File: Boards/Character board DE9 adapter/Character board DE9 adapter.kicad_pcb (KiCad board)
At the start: 2 copper layers, 22.1 x 35.3 mm, 3 parts, among them J1 DE9_Plug_MountingHoles, J2 character connector

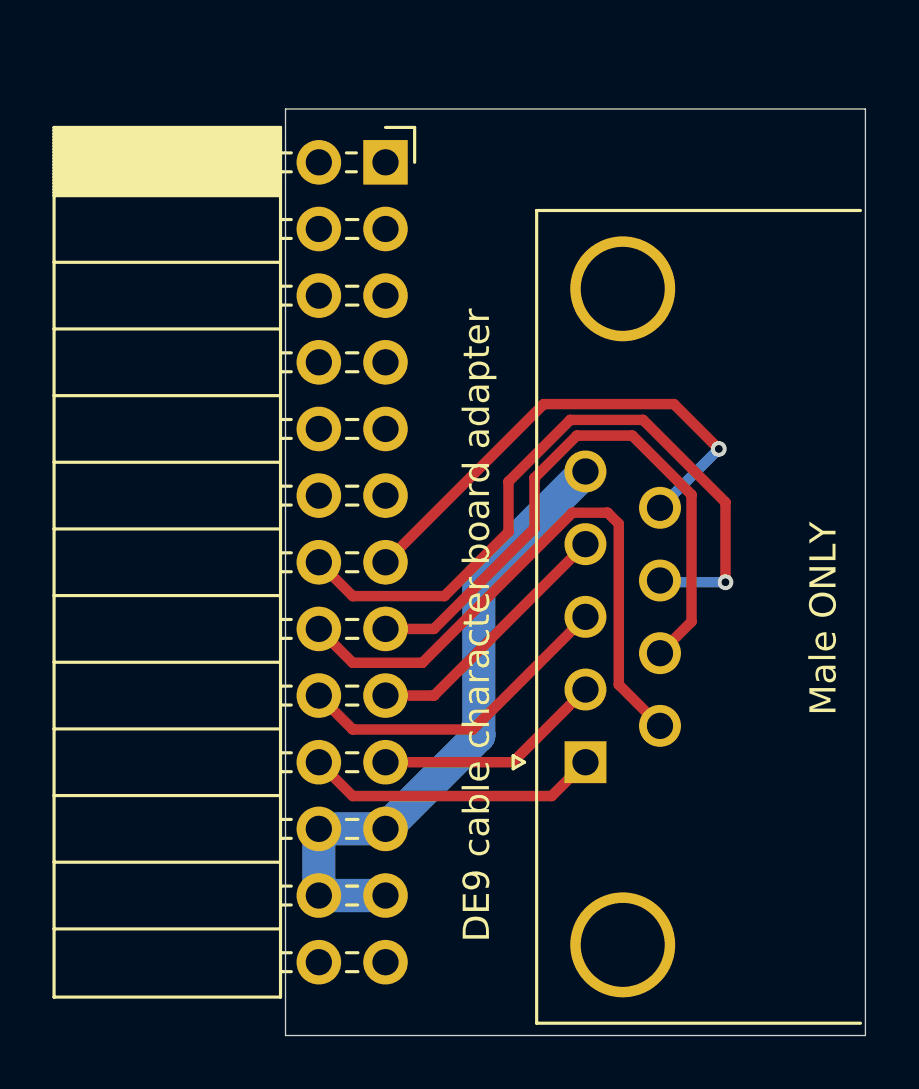
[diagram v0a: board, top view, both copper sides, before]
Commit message: added audio board schematics and de9 board fab files
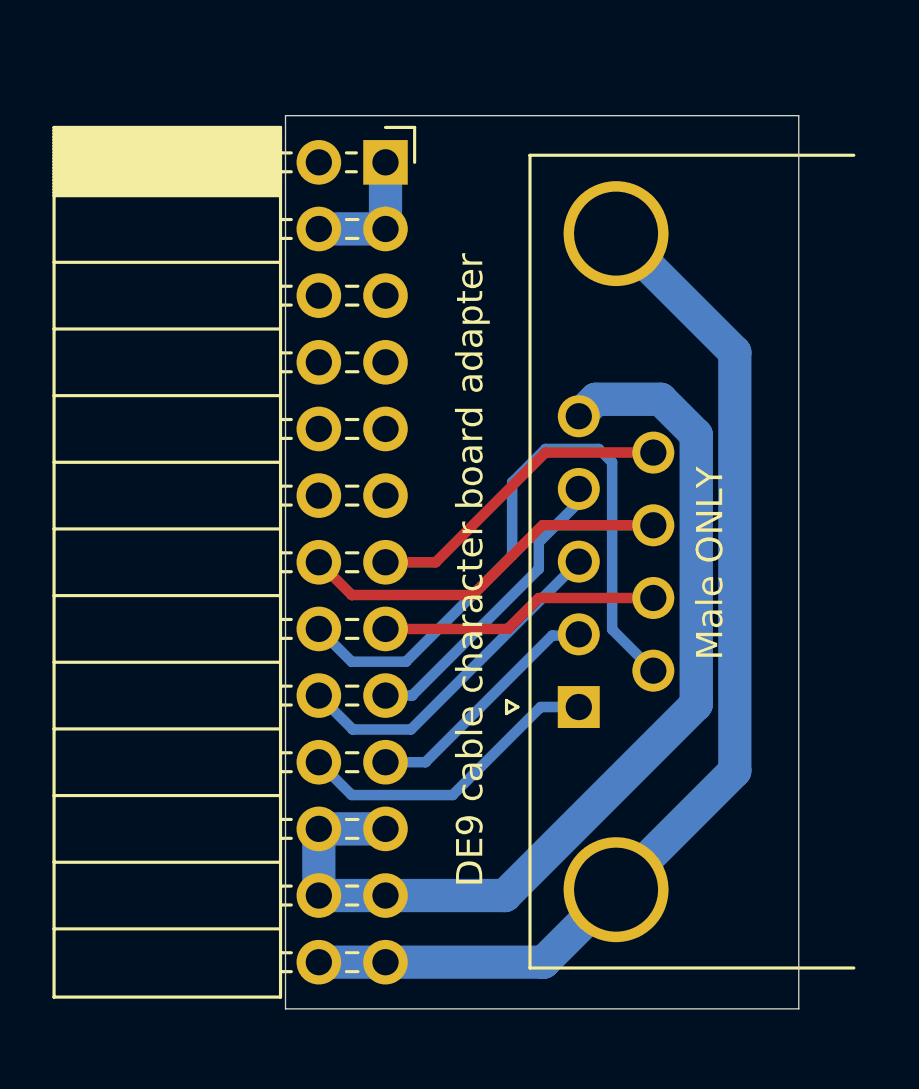
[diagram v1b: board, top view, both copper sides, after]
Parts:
- moved J1 2.12 mm to (121.7, 117.3)
- moved G*** 1.57 mm to (127.5, 97.5)
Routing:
- net 24R: track 0.00 -> 41.2 mm
- net +24VDC: track 24.4 -> 38.1 mm
- net CC6: track 23.3 -> 10.7 mm
- net CC7: track 26.8 -> 14.5 mm, vias 1 -> 0
- net CC8: track 19.1 -> 11.9 mm, vias 1 -> 0
- net SIGNAL GND.: track 0.00 -> 5.08 mm
- net CC5: track 22.9 -> 25.5 mm
- net CC4: track 10.0 -> 11.5 mm
- net CC3: track 12.5 -> 13.1 mm
- net CC2: track 8.77 -> 9.38 mm
- net CC1: track 11.2 -> 11.8 mm
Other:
- board size 22.1 x 35.3 mm -> 19.6 x 34 mm
